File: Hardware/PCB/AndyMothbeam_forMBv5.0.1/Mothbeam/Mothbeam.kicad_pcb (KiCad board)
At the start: 2 copper layers, 26.8 x 45 mm, 23 parts, among them CN1 X6511FRS-04-C85D30, SW2 SW_DIP_x04, U1 BCR421U, U2 BCR421U, U3 BCR421U

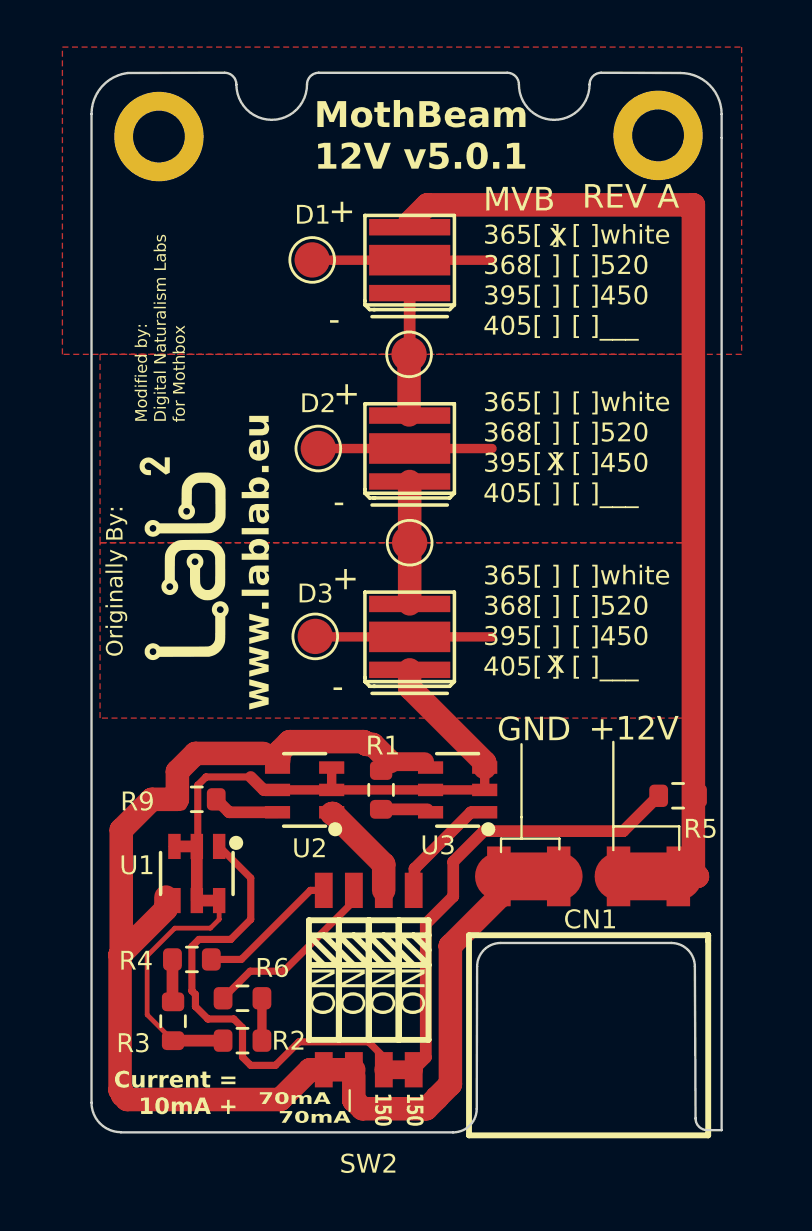
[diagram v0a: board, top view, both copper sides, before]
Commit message: Updated edge cut to make slightly wider and fix discontinuities
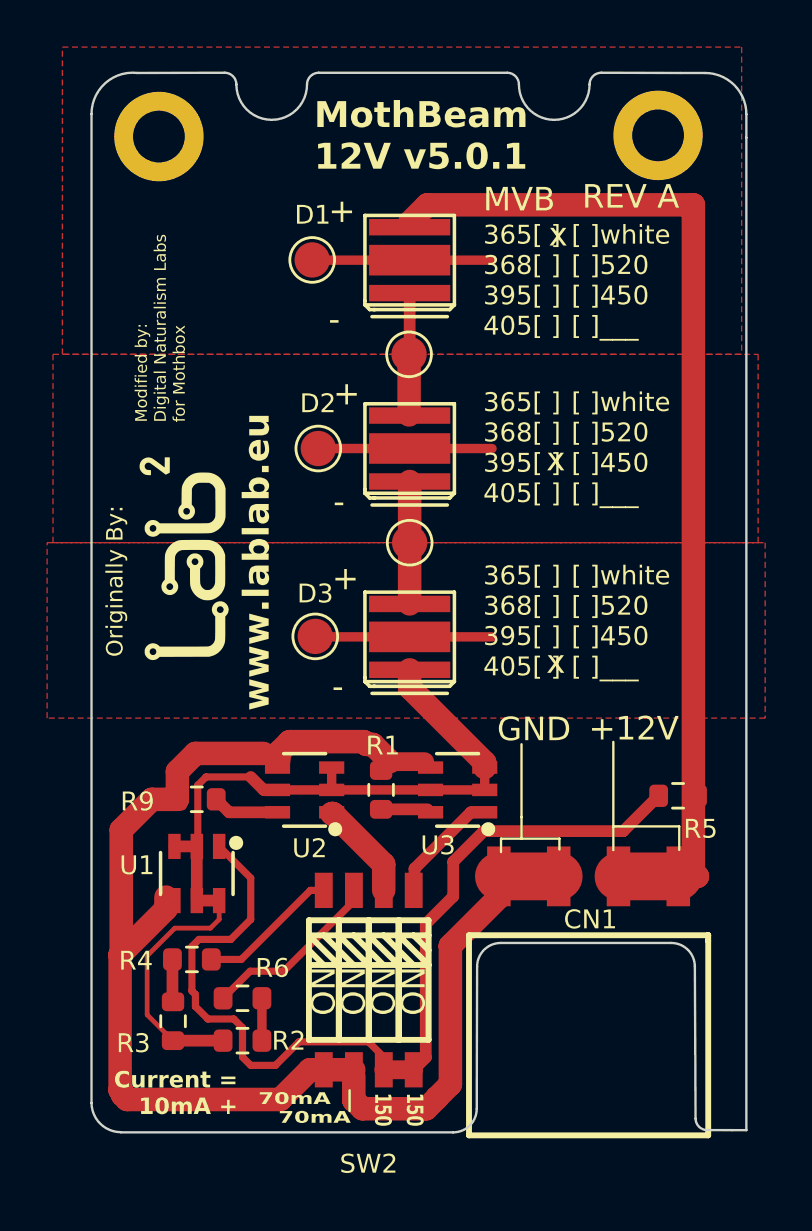
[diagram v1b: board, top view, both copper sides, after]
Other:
- board size 26.8 x 45 mm -> 27.8 x 45 mm
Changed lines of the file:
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@@
 	)
 	(gr_arc
-		(start 115.614656 67.947532)
+		(start 115.614653 67.951319)
 		(mid 115.909519 67.241205)
-		(end 116.617468 66.950256)
+		(end 116.623537 66.950292)
+		(stroke
+			(width 0.1)
+			(type solid)
+		)
+		(layer "Edge.Cuts")
+	)
+	(gr_line
+		(start 126.446121 74.90042)
+		(end 125.350032 74.89862)
 		(stroke
 			(width 0.1)
@@
 		(start 116.89 29.99)
 		(mid 117.24148 30.134386)
-		(end 117.389966 30.484154)
+		(end 117.389965 30.484154)
 		(stroke
 			(width 0.1)
@@
 	(gr_line
 		(start 99.237437 31.7374)
-		(end 99.237437 73.7373)
+		(end 99.237437 73.750716)
 		(stroke
 			(width 0.1)
@@
 	)
 	(gr_line
-		(start 104.89 29.99)
-		(end 100.778088 30)
+		(start 104.888784 29.990003)
+		(end 101.188258 29.999002)
 		(stroke
 			(width 0.1)
@@
 	)
 	(gr_arc
-		(start 104.89 29.99)
+		(start 104.888784 29.990003)
 		(mid 105.243553 30.136447)
 		(end 105.39 30.49)
@@
 	)
 	(gr_line
-		(start 114.588505 74.995152)
+		(start 114.588612 74.995152)
 		(end 100.4875 74.993719)
 		(stroke
@@
 	)
 	(gr_line
-		(start 126 32.75)
-		(end 126 31.75)
+		(start 127.05 32.75)
+		(end 127.05 31.75)
 		(stroke
 			(width 0.1)
@@
 	)
 	(gr_arc
-		(start 125.392317 74.90042)
+		(start 125.350032 74.89862)
 		(mid 125.038703 74.75388)
-		(end 124.89228 74.400217)
+		(end 124.892347 74.408397)
 		(stroke
 			(width 0.1)
@@
 		(start 120.39 30.49)
 		(mid 120.536447 30.136447)
-		(end 120.89 29.99)
+		(end 120.891488 29.990002)
 		(stroke
 			(width 0.1)
@@
 	)
 	(gr_arc
-		(start 123.868189 66.950292)
+		(start 123.852518 66.950334)
 		(mid 124.573852 67.246886)
-		(end 124.863108 67.955589)
+		(end 124.86302 67.936173)
 		(stroke
 			(width 0.1)
@@
 	)
 	(gr_arc
-		(start 120.390046 30.49)
+		(start 120.390045 30.49)
 		(mid 118.887077 31.990043)
-		(end 117.389965 30.484154)
+		(end 117.389968 30.484154)
 		(stroke
 			(width 0.1)
@@
 	)
 	(gr_arc
-		(start 115.598196 73.997873)
+		(start 115.598195 73.997922)
 		(mid 115.303414 74.704194)
-		(end 114.595527 74.995196)
+		(end 114.588612 74.995152)
 		(stroke
 			(width 0.1)
@@
 	)
 	(gr_line
-		(start 100.4875 74.987437)
-		(end 100.4875 75)
+		(start 100.4875 74.987435)
+		(end 100.4875 74.993719)
 		(stroke
 			(width 0.05)
@@
 	)
 	(gr_line
-		(start 125.997069 74.901407)
-		(end 125.396121 74.90042)
+		(start 127.05 74.901412)
+		(end 126.446121 74.90042)
 		(stroke
 			(width 0.1)
@@
 	)
 	(gr_line
-		(start 116.623531 66.950292)
-		(end 123.868189 66.950334)
+		(start 125.3 30)
+		(end 124.25 30)
 		(stroke
 			(width 0.1)
@@
 	)
 	(gr_line
-		(start 120.889919 29.99)
+		(start 116.623537 66.950292)
+		(end 123.852518 66.950334)
+		(stroke
+			(width 0.1)
+			(type solid)
+		)
+		(layer "Edge.Cuts")
+	)
+	(gr_line
+		(start 120.891488 29.990005)
 		(end 124.25 30)
 		(stroke
@@
 	)
 	(gr_arc
-		(start 124.25 30)
-		(mid 125.487437 30.512563)
-		(end 126 31.75)
+		(start 125.3 30)
+		(mid 126.537437 30.512563)
+		(end 127.05 31.75)
 		(stroke
 			(width 0.1)
@@
 	)
 	(gr_line
-		(start 124.863108 67.955589)
-		(end 124.892348 74.408566)
+		(start 124.86302 67.936173)
+		(end 124.892347 74.408397)
 		(stroke
 			(width 0.1)
@@
 	)
 	(gr_line
-		(start 126 74.901412)
-		(end 126 32.75)
+		(start 127.05 74.901412)
+		(end 127.05 32.75)
 		(stroke
 			(width 0.1)
@@
 	)
 	(gr_line
-		(start 115.598196 73.997921)
-		(end 115.614656 67.9503)
+		(start 115.598196 73.997922)
+		(end 115.614653 67.951319)
 		(stroke
 			(width 0.1)
@@
 	)
 	(gr_arc
-		(start 100.4875 74.987437)
+		(start 100.4875 74.987435)
 		(mid 99.60352 74.62128)
-		(end 99.237363 73.7373)
+		(end 99.237437 73.750716)
 		(stroke
 			(width 0.1)
@@
 		(start 99.237437 31.7374)
 		(mid 99.75 30.5)
-		(end 100.778088 30)
+		(end 101.188258 29.999002)
 		(stroke
 			(width 0.1)
@@
 	)
 	(zone
-		(net 9)
-		(net_name "/T2")
-		(layer "F.Cu")
-		(hatch edge 0.5)
-		(connect_pads
-			(clearance 0.35)
-		)
-		(min_thickness 0.25)
-		(filled_areas_thickness no)
-		(fill yes
-			(thermal_gap 0.5)
-			(thermal_bridge_width 0.5)
-			(smoothing chamfer)
-		)
-		(polygon
-			(pts
-				(xy 124.35 41.95) (xy 124.35 49.95) (xy 99.6 49.95) (xy 99.6 41.95)
-			)
-		)
-	)
-	(zone
-		(net 17)
-		(net_name "Net-(D2-A)")
+		(net 16)
+		(net_name "Net-(D1--)")
 		(layer "F.Cu")
 		(name "$teardrop_padvia$")
 		(hatch none 0.1)
-		(priority 30001)
+		(priority 30000)
 		(attr
 			(teardrop
@@
 		(polygon
 			(pts
-				(xy 113.25 48.464411) (xy 112.25 48.464411) (xy 112.014411 49.803682) (xy 112.75 49.951) (xy 113.485589 49.803682)
+				(xy 112.2246 43.435589) (xy 113.2246 43.435589) (xy 113.460189 42.096318) (xy 112.7246 41.949) (xy 111.989011 42.096318)
 			)
 		)
 	)
 	(zone
-		(net 16)
-		(net_name "Net-(D1--)")
+		(net 9)
+		(net_name "/T2")
+		(layer "F.Cu")
+		(hatch edge 0.5)
+		(connect_pads
+			(clearance 0.35)
+		)
+		(min_thickness 0.25)
+		(filled_areas_thickness no)
+		(fill yes
+			(thermal_gap 0.5)
+			(thermal_bridge_width 0.5)
+			(smoothing chamfer)
+		)
+		(polygon
+			(pts
+				(xy 127.55 41.95) (xy 127.55 49.95) (xy 97.6 49.95) (xy 97.6 41.95)
+			)
+		)
+	)
+	(zone
+		(net 17)
+		(net_name "Net-(D2-A)")
 		(layer "F.Cu")
 		(name "$teardrop_padvia$")
 		(hatch none 0.1)
-		(priority 30000)
+		(priority 30002)
 		(attr
 			(teardrop
@@
 		(polygon
 			(pts
-				(xy 112.2246 43.435589) (xy 113.2246 43.435589) (xy 113.460189 42.096318) (xy 112.7246 41.949) (xy 111.989011 42.096318)
+				(xy 112.25 51.435589) (xy 113.25 51.435589) (xy 113.485589 50.096318) (xy 112.75 49.949) (xy 112.014411 50.096318)
 			)
 		)
 	)
 	(zone
-		(net 17)
-		(net_name "Net-(D2-A)")
+		(net 16)
+		(net_name "Net-(D1--)")
 		(layer "F.Cu")
 		(name "$teardrop_padvia$")
 		(hatch none 0.1)
-		(priority 30002)
+		(priority 30003)
 		(attr
 			(teardrop
@@
 		(polygon
 			(pts
-				(xy 112.25 51.435589) (xy 113.25 51.435589) (xy 113.485589 50.096318) (xy 112.75 49.949) (xy 112.014411 50.096318)
+				(xy 113 40.464411) (xy 112.5 40.464411) (xy 111.989011 41.803682) (xy 112.7246 41.951) (xy 113.460189 41.803682)
 			)
 		)
@@
 	)
 	(zone
-		(net 10)
-		(net_name "/T3")
-		(layer "F.Cu")
-		(hatch edge 0.5)
-		(connect_pads
-			(clearance 0.35)
-		)
-		(min_thickness 0.25)
-		(filled_areas_thickness no)
-		(fill yes
-			(thermal_gap 0.5)
-			(thermal_bridge_width 0.5)
-			(smoothing chamfer)
-		)
-		(polygon
-			(pts
-				(xy 124.4 49.95) (xy 124.4 57.4) (xy 99.6 57.4) (xy 99.6 49.95)
-			)
-		)
-	)
-	(zone
-		(net 16)
-		(net_name "Net-(D1--)")
+		(net 17)
+		(net_name "Net-(D2-A)")
 		(layer "F.Cu")
 		(name "$teardrop_padvia$")
 		(hatch none 0.1)
-		(priority 30003)
+		(priority 30001)
 		(attr
 			(teardrop
@@
 		(polygon
 			(pts
-				(xy 113 40.464411) (xy 112.5 40.464411) (xy 111.989011 41.803682) (xy 112.7246 41.951) (xy 113.460189 41.803682)
-			)
-		)
+				(xy 113.25 48.464411) (xy 112.25 48.464411) (xy 112.014411 49.803682) (xy 112.75 49.951) (xy 113.485589 49.803682)
+			)
+		)
+	)
+	(zone
+		(net 10)
+		(net_name "/T3")
+		(layer "F.Cu")
+		(hatch edge 0.5)
+		(connect_pads
+			(clearance 0.35)
+		)
+		(min_thickness 0.25)
+		(filled_areas_thickness no)
+		(fill yes
+			(thermal_gap 0.5)
+			(thermal_bridge_width 0.5)
+			(smoothing chamfer)
+		)
+		(polygon
+			(pts
+				(xy 127.85 49.95) (xy 127.85 57.4) (xy 97.35 57.4) (xy 97.35 49.95)
+			)
+		)
